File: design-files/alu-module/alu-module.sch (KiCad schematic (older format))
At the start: 34 parts, among them U302 74LS382A, U303 74HCT377, U304 74HCT245, U305 74HCT08, U306 74LS382A, U307 4002

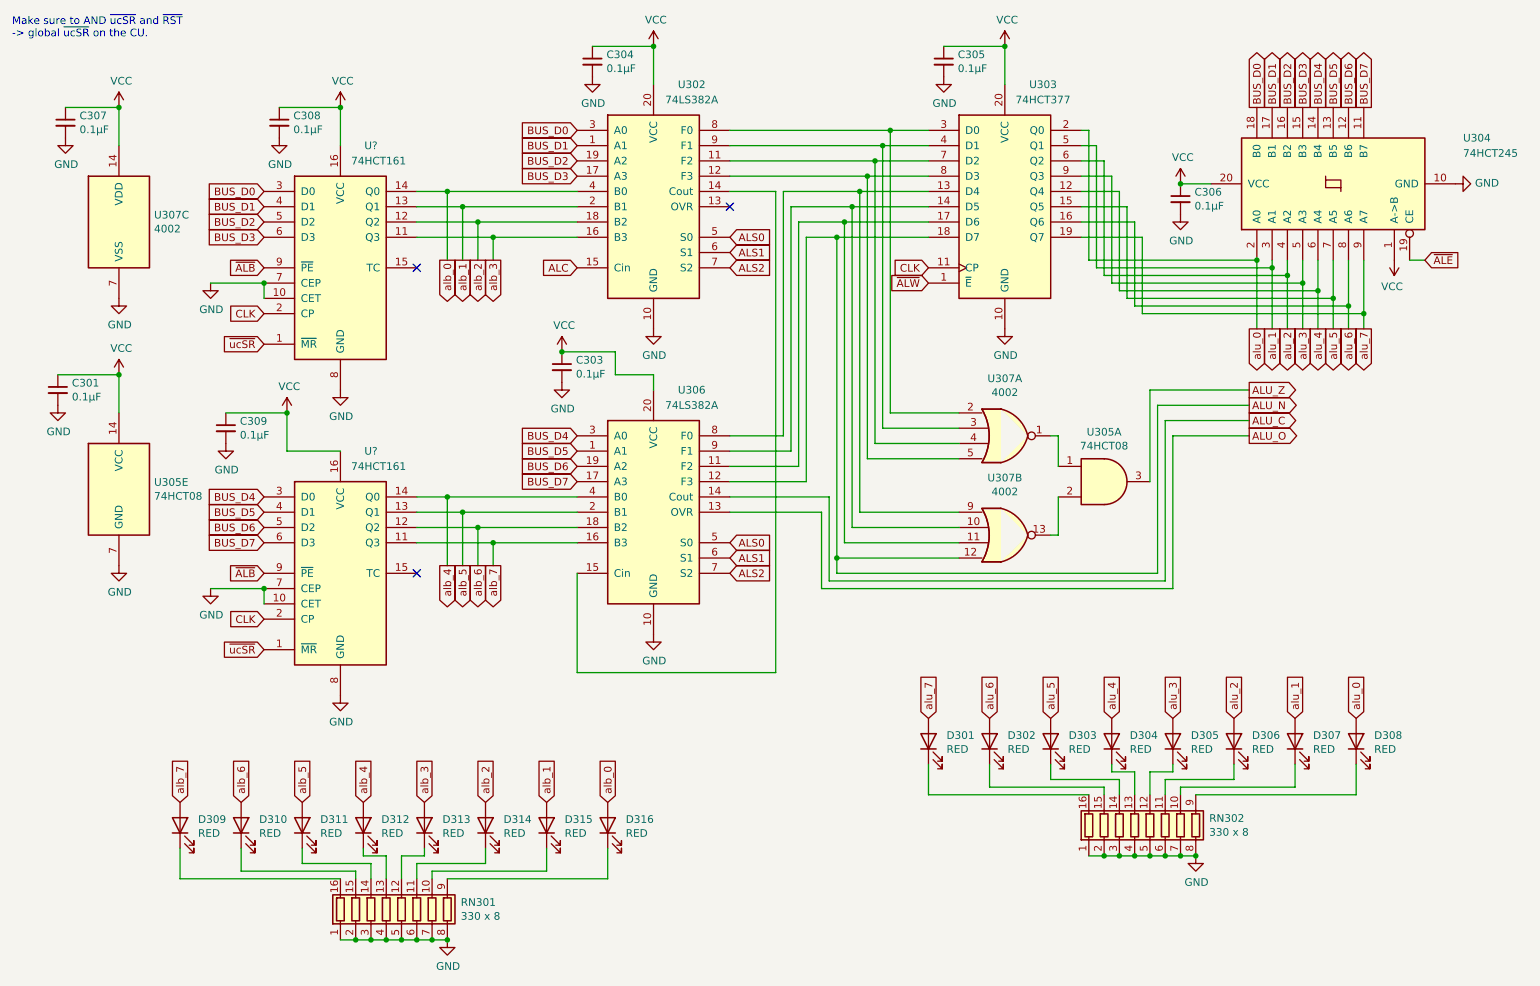
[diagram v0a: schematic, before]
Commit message: Re-annotate ICs on the ALU module.
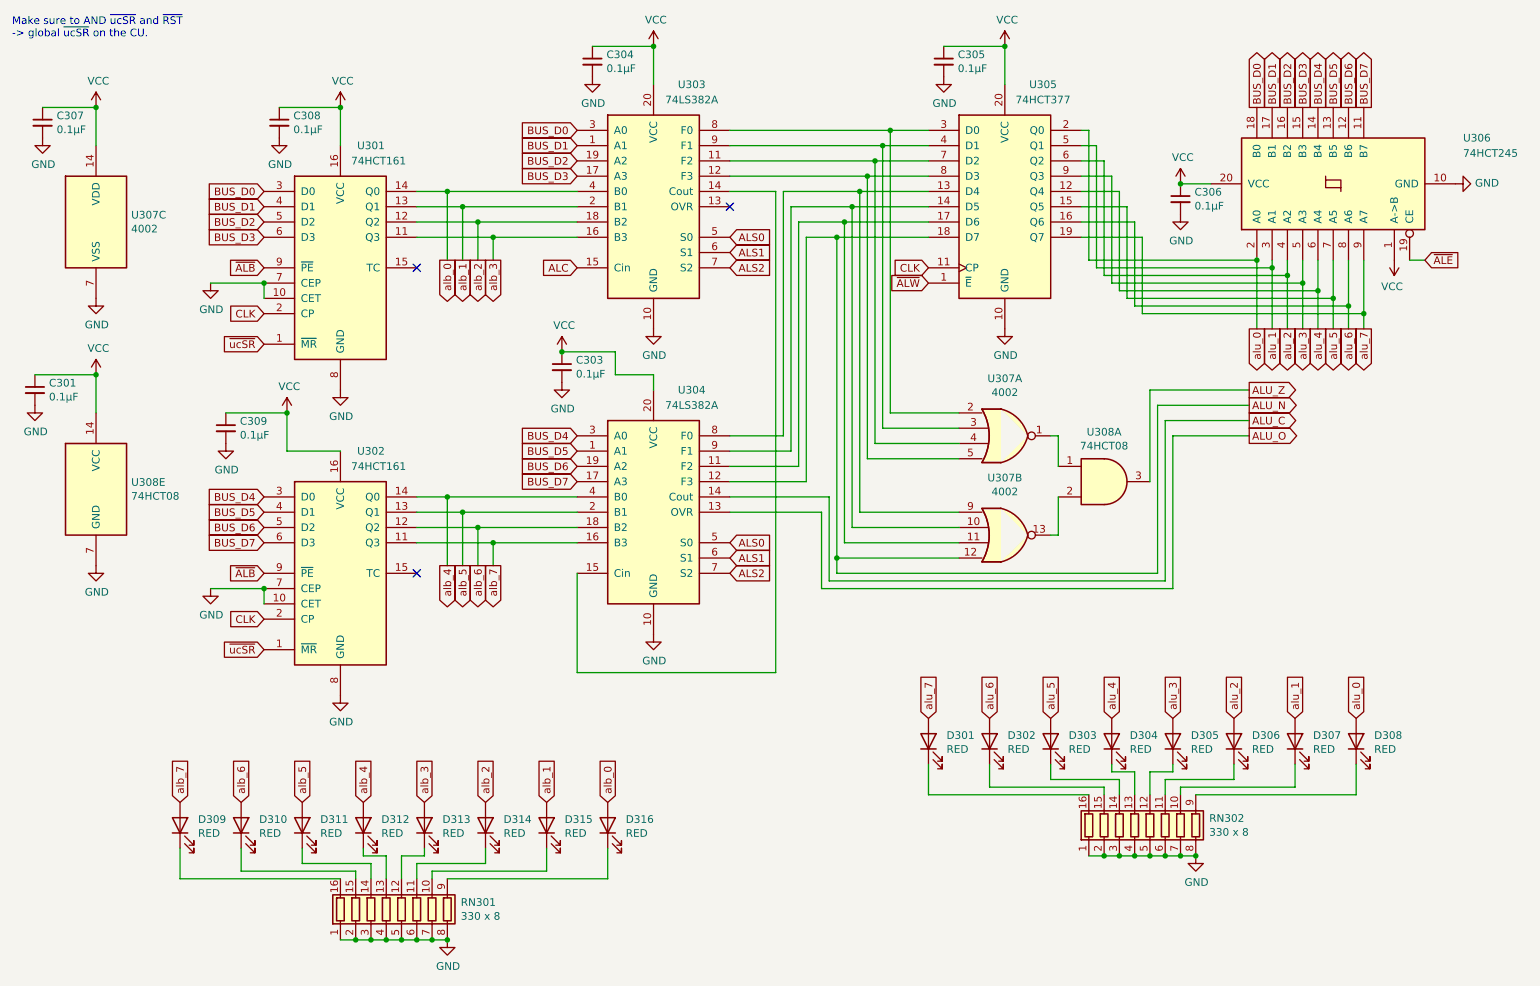
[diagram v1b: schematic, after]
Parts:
- gave numbers to parts that had none: 2
- renumbered U302 to U303, U306 to U304, U303 to U305, U304 to U306, U305 to U308
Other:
- moved on the sheet: C301, C307, U307C, U308E
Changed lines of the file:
@@
 Make sure to AND ~ucSR~ and ~RST~\n-> global ~ucSR~ on the CU.
 $Comp
-L jrt-ICs:74LS382A U302
+L jrt-ICs:74LS382A U303
 U 1 1 64133219
 P 4750 1850
-F 0 "U302" H 5000 2650 50  0000 C CNN
+F 0 "U303" H 5000 2650 50  0000 C CNN
 F 1 "74LS382A" H 5000 2550 50  0000 C CNN
 F 2 "Package_DIP:DIP-20_W7.62mm_Socket" H 5400 1150 50  0001 C CNN
@@
 BUS_D3
 $Comp
-L jrt-ICs:74LS382A U306
+L jrt-ICs:74LS382A U304
 U 1 1 6413A5F9
 P 4750 3850
-F 0 "U306" H 5000 4650 50  0000 C CNN
+F 0 "U304" H 5000 4650 50  0000 C CNN
 F 1 "74LS382A" H 5000 4550 50  0000 C CNN
 F 2 "Package_DIP:DIP-20_W7.62mm_Socket" H 5400 3150 50  0001 C CNN
@@
 NoConn ~ 5250 1850
 $Comp
-L 74xx:74LS377 U303
+L 74xx:74LS377 U305
 U 1 1 641403CB
 P 7050 1850
-F 0 "U303" H 7300 2650 50  0000 C CNN
+F 0 "U305" H 7300 2650 50  0000 C CNN
 F 1 "74HCT377" H 7300 2550 50  0000 C CNN
 F 2 "Package_DIP:DIP-20_W7.62mm_Socket" H 7050 1850 50  0001 C CNN
@@
 	5950 2050 6550 2050
 $Comp
-L 74xx:74LS08 U305
+L 74xx:74LS08 U308
 U 1 1 6417242F
 P 7700 3650
-F 0 "U305" H 7700 3975 50  0000 C CNN
+F 0 "U308" H 7700 3975 50  0000 C CNN
 F 1 "74HCT08" H 7700 3884 50  0000 C CNN
 F 2 "Package_DIP:DIP-14_W7.62mm_Socket" H 7700 3650 50  0001 C CNN
@@
 ALU_O
 $Comp
-L 74xx:74LS245 U304
+L 74xx:74LS245 U306
 U 1 1 6419D514
 P 9200 1700
-F 0 "U304" V 9500 850 50  0000 R CNN
+F 0 "U306" V 9500 850 50  0000 R CNN
 F 1 "74HCT245" V 9400 850 50  0000 R CNN
 F 2 "Package_DIP:DIP-20_W7.62mm_Socket" H 9200 1700 50  0001 C CNN
@@
 Connection ~ 8700 2200
 $Comp
-L 74xx:74LS08 U305
+L 74xx:74LS08 U308
 U 5 1 6422D9BB
-P 1250 3700
-F 0 "U305" H 1480 3746 50  0000 L CNN
-F 1 "74HCT08" H 1480 3655 50  0000 L CNN
-F 2 "Package_DIP:DIP-14_W7.62mm_Socket" H 1250 3700 50  0001 C CNN
-F 3 "http://www.ti.com/lit/gpn/sn74LS08" H 1250 3700 50  0001 C CNN
-	5    1250 3700
+P 1100 3700
+F 0 "U308" H 1330 3746 50  0000 L CNN
+F 1 "74HCT08" H 1330 3655 50  0000 L CNN
+F 2 "Package_DIP:DIP-14_W7.62mm_Socket" H 1100 3700 50  0001 C CNN
+F 3 "http://www.ti.com/lit/gpn/sn74LS08" H 1100 3700 50  0001 C CNN
+	5    1100 3700
 	1    0    0    -1
 $EndComp
@@
 L power:GND #PWR0106
 U 1 1 642303D4
-P 1250 4200
-F 0 "#PWR0106" H 1250 3950 50  0001 C CNN
-F 1 "GND" H 1255 4027 50  0000 C CNN
-F 2 "" H 1250 4200 50  0001 C CNN
-F 3 "" H 1250 4200 50  0001 C CNN
-	1    1250 4200
+P 1100 4200
+F 0 "#PWR0106" H 1100 3950 50  0001 C CNN
+F 1 "GND" H 1105 4027 50  0000 C CNN
+F 2 "" H 1100 4200 50  0001 C CNN
+F 3 "" H 1100 4200 50  0001 C CNN
+	1    1100 4200
 	1    0    0    -1
 $EndComp
@@
 L 4xxx:4002 U307
 U 3 1 6423095A
-P 1250 1950
-F 0 "U307" H 1480 1996 50  0000 L CNN
-F 1 "4002" H 1480 1905 50  0000 L CNN
-F 2 "Package_DIP:DIP-14_W7.62mm_Socket" H 1250 1950 50  0001 C CNN
-F 3 "http://www.intersil.com/content/dam/Intersil/documents/cd40/cd4000bms-01bms-02bms-25bms.pdf" H 1250 1950 50  0001 C CNN
-	3    1250 1950
+P 1100 1950
+F 0 "U307" H 1330 1996 50  0000 L CNN
+F 1 "4002" H 1330 1905 50  0000 L CNN
+F 2 "Package_DIP:DIP-14_W7.62mm_Socket" H 1100 1950 50  0001 C CNN
+F 3 "http://www.intersil.com/content/dam/Intersil/documents/cd40/cd4000bms-01bms-02bms-25bms.pdf" H 1100 1950 50  0001 C CNN
+	3    1100 1950
 	1    0    0    -1
 $EndComp
@@
 L power:GND #PWR0107
 U 1 1 64234DC9
-P 1250 2450
-F 0 "#PWR0107" H 1250 2200 50  0001 C CNN
-F 1 "GND" H 1255 2277 50  0000 C CNN
-F 2 "" H 1250 2450 50  0001 C CNN
-F 3 "" H 1250 2450 50  0001 C CNN
-	1    1250 2450
+P 1100 2450
+F 0 "#PWR0107" H 1100 2200 50  0001 C CNN
+F 1 "GND" H 1105 2277 50  0000 C CNN
+F 2 "" H 1100 2450 50  0001 C CNN
+F 3 "" H 1100 2450 50  0001 C CNN
+	1    1100 2450
 	1    0    0    -1
 $EndComp
@@
 L Device:C_Small C301
 U 1 1 6425F817
-P 850 3050
-F 0 "C301" H 942 3096 50  0000 L CNN
-F 1 "0.1µF" H 942 3005 50  0000 L CNN
-F 2 "Capacitor_THT:C_Radial_D6.3mm_H5.0mm_P2.50mm" H 850 3050 50  0001 C CNN
-F 3 "~" H 850 3050 50  0001 C CNN
-F 4 "80-C320C104K2R5TA" H 850 3050 50  0001 C CNN "Mouser"
-	1    850  3050
+P 700 3050
+F 0 "C301" H 792 3096 50  0000 L CNN
+F 1 "0.1µF" H 792 3005 50  0000 L CNN
+F 2 "Capacitor_THT:C_Radial_D6.3mm_H5.0mm_P2.50mm" H 700 3050 50  0001 C CNN
+F 3 "~" H 700 3050 50  0001 C CNN
+F 4 "80-C320C104K2R5TA" H 700 3050 50  0001 C CNN "Mouser"
+	1    700  3050
 	1    0    0    -1
 $EndComp
@@
 L Device:C_Small C307
 U 1 1 642627E3
-P 900 1300
-F 0 "C307" H 992 1346 50  0000 L CNN
-F 1 "0.1µF" H 992 1255 50  0000 L CNN
-F 2 "Capacitor_THT:C_Radial_D6.3mm_H5.0mm_P2.50mm" H 900 1300 50  0001 C CNN
-F 3 "~" H 900 1300 50  0001 C CNN
-F 4 "80-C320C104K2R5TA" H 900 1300 50  0001 C CNN "Mouser"
-	1    900  1300
+P 750 1300
+F 0 "C307" H 842 1346 50  0000 L CNN
+F 1 "0.1µF" H 842 1255 50  0000 L CNN
+F 2 "Capacitor_THT:C_Radial_D6.3mm_H5.0mm_P2.50mm" H 750 1300 50  0001 C CNN
+F 3 "~" H 750 1300 50  0001 C CNN
+F 4 "80-C320C104K2R5TA" H 750 1300 50  0001 C CNN "Mouser"
+	1    750  1300
 	1    0    0    -1
 $EndComp
@@
 L power:GND #PWR0119
 U 1 1 64264EFC
-P 850 3150
-F 0 "#PWR0119" H 850 2900 50  0001 C CNN
-F 1 "GND" H 855 2977 50  0000 C CNN
-F 2 "" H 850 3150 50  0001 C CNN
-F 3 "" H 850 3150 50  0001 C CNN
-	1    850  3150
+P 700 3150
+F 0 "#PWR0119" H 700 2900 50  0001 C CNN
+F 1 "GND" H 705 2977 50  0000 C CNN
+F 2 "" H 700 3150 50  0001 C CNN
+F 3 "" H 700 3150 50  0001 C CNN
+	1    700  3150
 	1    0    0    -1
 $EndComp
@@
 L power:GND #PWR0121
 U 1 1 6426E60F
-P 900 1400
-F 0 "#PWR0121" H 900 1150 50  0001 C CNN
-F 1 "GND" H 905 1227 50  0000 C CNN
-F 2 "" H 900 1400 50  0001 C CNN
-F 3 "" H 900 1400 50  0001 C CNN
-	1    900  1400
+P 750 1400
+F 0 "#PWR0121" H 750 1150 50  0001 C CNN
+F 1 "GND" H 755 1227 50  0000 C CNN
+F 2 "" H 750 1400 50  0001 C CNN
+F 3 "" H 750 1400 50  0001 C CNN
+	1    750  1400
 	1    0    0    -1
 $EndComp
@@
 	7050 800  6650 800
 Wire Wire Line
-	1250 3200 1250 2950
-Wire Wire Line
-	1250 2950 850  2950
+	1100 3200 1100 2950
+Wire Wire Line
+	1100 2950 700  2950
 Wire Wire Line
 	4750 3050 4750 2950
@@
 	8400 1700 8200 1700
 Wire Wire Line
-	1250 1450 1250 1200
-Wire Wire Line
-	1250 1200 900  1200
+	1100 1450 1100 1200
+Wire Wire Line
+	1100 1200 750  1200
 Wire Wire Line
 	4750 800  4350 800
@@
 L power:VCC #PWR0128
 U 1 1 6429A94D
-P 1250 1200
-F 0 "#PWR0128" H 1250 1050 50  0001 C CNN
-F 1 "VCC" H 1265 1373 50  0000 C CNN
-F 2 "" H 1250 1200 50  0001 C CNN
-F 3 "" H 1250 1200 50  0001 C CNN
-	1    1250 1200
-	1    0    0    -1
-$EndComp
-Connection ~ 1250 1200
+P 1100 1200
+F 0 "#PWR0128" H 1100 1050 50  0001 C CNN
+F 1 "VCC" H 1115 1373 50  0000 C CNN
+F 2 "" H 1100 1200 50  0001 C CNN
+F 3 "" H 1100 1200 50  0001 C CNN
+	1    1100 1200
+	1    0    0    -1
+$EndComp
+Connection ~ 1100 1200
 $Comp
 L power:VCC #PWR0129
@@
 L power:VCC #PWR0130
 U 1 1 6429B977
-P 1250 2950
-F 0 "#PWR0130" H 1250 2800 50  0001 C CNN
-F 1 "VCC" H 1265 3123 50  0000 C CNN
-F 2 "" H 1250 2950 50  0001 C CNN
-F 3 "" H 1250 2950 50  0001 C CNN
-	1    1250 2950
-	1    0    0    -1
-$EndComp
-Connection ~ 1250 2950
+P 1100 2950
+F 0 "#PWR0130" H 1100 2800 50  0001 C CNN
+F 1 "VCC" H 1115 3123 50  0000 C CNN
+F 2 "" H 1100 2950 50  0001 C CNN
+F 3 "" H 1100 2950 50  0001 C CNN
+	1    1100 2950
+	1    0    0    -1
+$EndComp
+Connection ~ 1100 2950
 $Comp
 L Device:C_Small C308
@@
 Connection ~ 3400 6650
 $Comp
-L 74xx:74LS161 U?
+L 74xx:74LS161 U301
 U 1 1 622FC59D
 P 2700 2250
-F 0 "U?" H 2900 3050 50  0000 C CNN
+F 0 "U301" H 2900 3050 50  0000 C CNN
 F 1 "74HCT161" H 2950 2950 50  0000 C CNN
 F 2 "" H 2700 2250 50  0001 C CNN
@@
 Connection ~ 2200 2350
 $Comp
-L 74xx:74LS161 U?
+L 74xx:74LS161 U302
 U 1 1 622FE2BB
 P 2700 4250
-F 0 "U?" H 2900 5050 50  0000 C CNN
+F 0 "U302" H 2900 5050 50  0000 C CNN
 F 1 "74HCT161" H 2950 4950 50  0000 C CNN
 F 2 "" H 2700 4250 50  0001 C CNN

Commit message: Re-annotate the LEDs on the ALU module.
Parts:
- renumbered D309 to D301, D310 to D302, D311 to D303, D312 to D304, D313 to D305, D314 to D306, D315 to D307, D316 to D308, D301 to D309, D302 to D310, D303 to D311, D304 to D312, D305 to D313, D306 to D314, D307 to D315, D308 to D316
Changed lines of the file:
@@
 $EndComp
 $Comp
-L Device:LED D301
+L Device:LED D309
 U 1 1 64235BB1
 P 6550 5350
-F 0 "D301" V 6589 5232 50  0000 R CNN
+F 0 "D309" V 6589 5232 50  0000 R CNN
 F 1 "RED" V 6498 5232 50  0000 R CNN
 F 2 "LED_THT:LED_D5.0mm" H 6550 5350 50  0001 C CNN
@@
 $EndComp
 $Comp
-L Device:LED D302
+L Device:LED D310
 U 1 1 642361E5
 P 6950 5350
-F 0 "D302" V 6989 5232 50  0000 R CNN
+F 0 "D310" V 6989 5232 50  0000 R CNN
 F 1 "RED" V 6898 5232 50  0000 R CNN
 F 2 "LED_THT:LED_D5.0mm" H 6950 5350 50  0001 C CNN
@@
 $EndComp
 $Comp
-L Device:LED D303
+L Device:LED D311
 U 1 1 64236303
 P 7350 5350
-F 0 "D303" V 7389 5232 50  0000 R CNN
+F 0 "D311" V 7389 5232 50  0000 R CNN
 F 1 "RED" V 7298 5232 50  0000 R CNN
 F 2 "LED_THT:LED_D5.0mm" H 7350 5350 50  0001 C CNN
@@
 $EndComp
 $Comp
-L Device:LED D304
+L Device:LED D312
 U 1 1 64236436
 P 7750 5350
-F 0 "D304" V 7789 5232 50  0000 R CNN
+F 0 "D312" V 7789 5232 50  0000 R CNN
 F 1 "RED" V 7698 5232 50  0000 R CNN
 F 2 "LED_THT:LED_D5.0mm" H 7750 5350 50  0001 C CNN
@@
 $EndComp
 $Comp
-L Device:LED D305
+L Device:LED D313
 U 1 1 64236569
 P 8150 5350
-F 0 "D305" V 8189 5232 50  0000 R CNN
+F 0 "D313" V 8189 5232 50  0000 R CNN
 F 1 "RED" V 8098 5232 50  0000 R CNN
 F 2 "LED_THT:LED_D5.0mm" H 8150 5350 50  0001 C CNN
@@
 $EndComp
 $Comp
-L Device:LED D306
+L Device:LED D314
 U 1 1 6423669C
 P 8550 5350
-F 0 "D306" V 8589 5232 50  0000 R CNN
+F 0 "D314" V 8589 5232 50  0000 R CNN
 F 1 "RED" V 8498 5232 50  0000 R CNN
 F 2 "LED_THT:LED_D5.0mm" H 8550 5350 50  0001 C CNN
@@
 $EndComp
 $Comp
-L Device:LED D307
+L Device:LED D315
 U 1 1 642367CF
 P 8950 5350
-F 0 "D307" V 8989 5232 50  0000 R CNN
+F 0 "D315" V 8989 5232 50  0000 R CNN
 F 1 "RED" V 8898 5232 50  0000 R CNN
 F 2 "LED_THT:LED_D5.0mm" H 8950 5350 50  0001 C CNN
@@
 $EndComp
 $Comp
-L Device:LED D308
+L Device:LED D316
 U 1 1 64236902
 P 9350 5350
-F 0 "D308" V 9389 5232 50  0000 R CNN
+F 0 "D316" V 9389 5232 50  0000 R CNN
 F 1 "RED" V 9298 5232 50  0000 R CNN
 F 2 "LED_THT:LED_D5.0mm" H 9350 5350 50  0001 C CNN
@@
 	5600 1750 5600 3350
 $Comp
-L Device:LED D309
+L Device:LED D301
 U 1 1 622A7146
 P 1650 5900
-F 0 "D309" V 1689 5782 50  0000 R CNN
+F 0 "D301" V 1689 5782 50  0000 R CNN
 F 1 "RED" V 1598 5782 50  0000 R CNN
 F 2 "LED_THT:LED_D5.0mm" H 1650 5900 50  0001 C CNN
@@
 $EndComp
 $Comp
-L Device:LED D310
+L Device:LED D302
 U 1 1 622A714D
 P 2050 5900
-F 0 "D310" V 2089 5782 50  0000 R CNN
+F 0 "D302" V 2089 5782 50  0000 R CNN
 F 1 "RED" V 1998 5782 50  0000 R CNN
 F 2 "LED_THT:LED_D5.0mm" H 2050 5900 50  0001 C CNN
@@
 $EndComp
 $Comp
-L Device:LED D311
+L Device:LED D303
 U 1 1 622A7154
 P 2450 5900
-F 0 "D311" V 2489 5782 50  0000 R CNN
+F 0 "D303" V 2489 5782 50  0000 R CNN
 F 1 "RED" V 2398 5782 50  0000 R CNN
 F 2 "LED_THT:LED_D5.0mm" H 2450 5900 50  0001 C CNN
@@
 $EndComp
 $Comp
-L Device:LED D312
+L Device:LED D304
 U 1 1 622A715B
 P 2850 5900
-F 0 "D312" V 2889 5782 50  0000 R CNN
+F 0 "D304" V 2889 5782 50  0000 R CNN
 F 1 "RED" V 2798 5782 50  0000 R CNN
 F 2 "LED_THT:LED_D5.0mm" H 2850 5900 50  0001 C CNN
@@
 $EndComp
 $Comp
-L Device:LED D313
+L Device:LED D305
 U 1 1 622A7162
 P 3250 5900
-F 0 "D313" V 3289 5782 50  0000 R CNN
+F 0 "D305" V 3289 5782 50  0000 R CNN
 F 1 "RED" V 3198 5782 50  0000 R CNN
 F 2 "LED_THT:LED_D5.0mm" H 3250 5900 50  0001 C CNN
@@
 $EndComp
 $Comp
-L Device:LED D314
+L Device:LED D306
 U 1 1 622A7169
 P 3650 5900
-F 0 "D314" V 3689 5782 50  0000 R CNN
+F 0 "D306" V 3689 5782 50  0000 R CNN
 F 1 "RED" V 3598 5782 50  0000 R CNN
 F 2 "LED_THT:LED_D5.0mm" H 3650 5900 50  0001 C CNN
@@
 $EndComp
 $Comp
-L Device:LED D315
+L Device:LED D307
 U 1 1 622A7170
 P 4050 5900
-F 0 "D315" V 4089 5782 50  0000 R CNN
+F 0 "D307" V 4089 5782 50  0000 R CNN
 F 1 "RED" V 3998 5782 50  0000 R CNN
 F 2 "LED_THT:LED_D5.0mm" H 4050 5900 50  0001 C CNN
@@
 $EndComp
 $Comp
-L Device:LED D316
+L Device:LED D308
 U 1 1 622A7177
 P 4450 5900
-F 0 "D316" V 4489 5782 50  0000 R CNN
+F 0 "D308" V 4489 5782 50  0000 R CNN
 F 1 "RED" V 4398 5782 50  0000 R CNN
 F 2 "LED_THT:LED_D5.0mm" H 4450 5900 50  0001 C CNN
